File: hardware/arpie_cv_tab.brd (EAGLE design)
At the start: 35.9 x 57.2 mm, 63 parts, among them IC1 MCP4726, IC2 MCP601OT, IC3 LM27675M5_CHARGEPUMP, IC4 LM358D, IC5 LM4041A12DBZ, IC6 24LC_16BT-I/OT

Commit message: add values to schematic
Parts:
- R11, R8: value (none) -> 2m2
- R4, R5: value (none) -> 1k
- R6: value 100k -> 47k
- R7: value (none) -> 47k
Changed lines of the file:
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@@
 <attribute name="VALUE" x="82.804" y="31.496" size="1.27" layer="27" rot="R180"/>
 </element>
-<element name="R5" library="rcl" package="R0805" value="" x="81.915" y="22.86" smashed="yes">
+<element name="R5" library="rcl" package="R0805" value="1k" x="81.915" y="22.86" smashed="yes">
 <attribute name="NAME" x="77.597" y="22.987" size="1.27" layer="25" font="vector" ratio="20"/>
 </element>
-<element name="R4" library="rcl" package="R0805" value="" x="81.915" y="31.75" smashed="yes">
+<element name="R4" library="rcl" package="R0805" value="1k" x="81.915" y="31.75" smashed="yes">
 <attribute name="NAME" x="77.724" y="30.353" size="1.27" layer="25" font="vector" ratio="20"/>
 </element>
@@
 <attribute name="NAME" x="77.597" y="11.43" size="1.27" layer="25" font="vector" ratio="20" rot="R90"/>
 </element>
-<element name="R7" library="rcl" package="R0805" value="" x="67.31" y="15.24" smashed="yes" rot="R270">
+<element name="R7" library="rcl" package="R0805" value="47k" x="67.31" y="15.24" smashed="yes" rot="R270">
 <attribute name="NAME" x="64.77" y="11.938" size="1.27" layer="25" font="vector" ratio="20"/>
-<attribute name="VALUE" x="64.77" y="15.875" size="1.27" layer="27" rot="R270"/>
 </element>
-<element name="R6" library="rcl" package="R0805" value="100k" x="64.77" y="15.24" smashed="yes" rot="R90">
+<element name="R6" library="rcl" package="R0805" value="47k" x="64.77" y="15.24" smashed="yes" rot="R90">
 <attribute name="NAME" x="62.23" y="16.637" size="1.27" layer="25" font="vector" ratio="20" rot="R270"/>
 </element>
@@
 <attribute name="NAME" x="80.899" y="18.415" size="1.27" layer="25" font="vector" ratio="20"/>
 </element>
-<element name="R8" library="rcl" package="R0805" value="" x="79.375" y="16.129" smashed="yes" rot="R90">
+<element name="R8" library="rcl" package="R0805" value="2m2" x="79.375" y="16.129" smashed="yes" rot="R90">
 <attribute name="NAME" x="76.835" y="18.161" size="1.27" layer="25" font="vector" ratio="20" rot="R270"/>
-<attribute name="VALUE" x="81.915" y="15.494" size="1.27" layer="27" rot="R90"/>
 </element>
-<element name="R11" library="rcl" package="R0805" value="" x="79.375" y="8.89" smashed="yes" rot="R270">
+<element name="R11" library="rcl" package="R0805" value="2m2" x="79.375" y="8.89" smashed="yes" rot="R270">
 <attribute name="NAME" x="77.724" y="5.461" size="1.27" layer="25" font="vector" ratio="20"/>
-<attribute name="VALUE" x="76.835" y="9.525" size="1.27" layer="27" rot="R270"/>
 </element>
 <element name="C10" library="resistor" package="C0805" value="" x="69.85" y="15.24" smashed="yes" rot="R90">

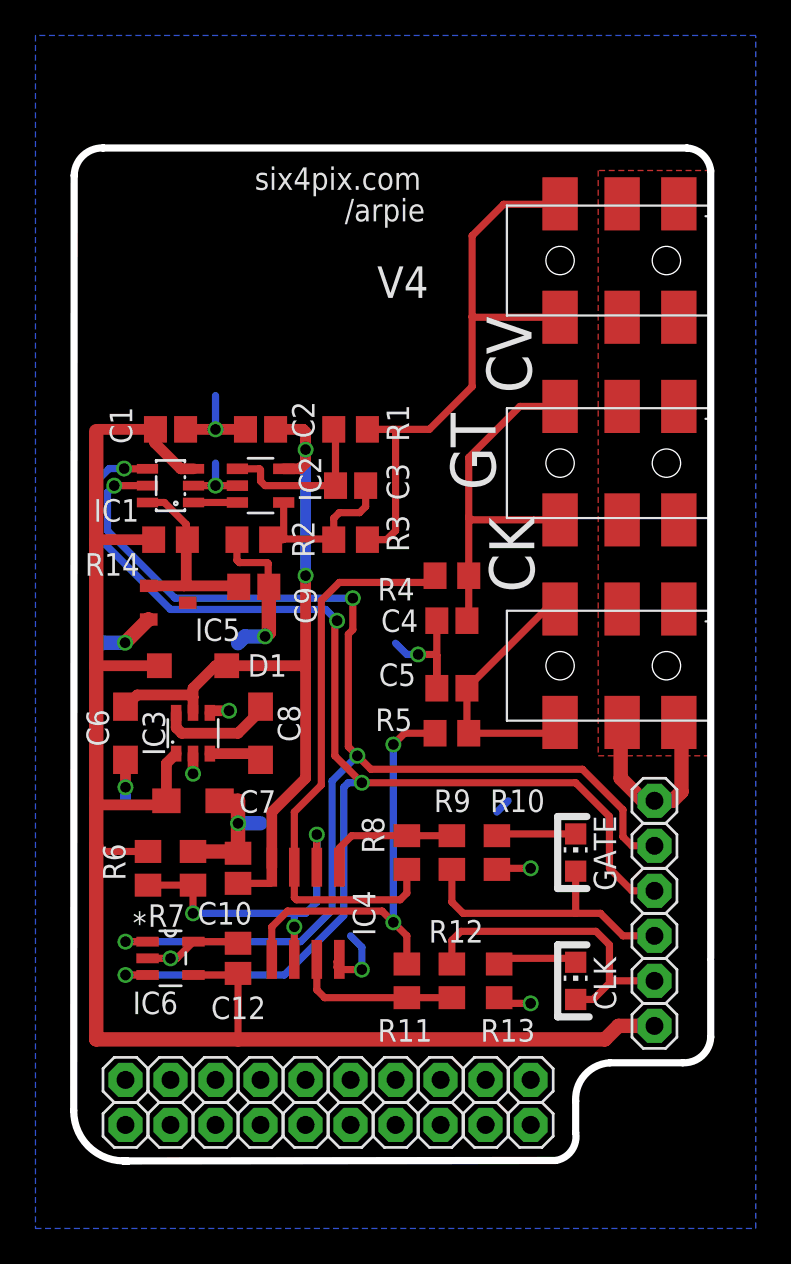
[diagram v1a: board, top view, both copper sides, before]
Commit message: V5 - change type of 3.5mm socket
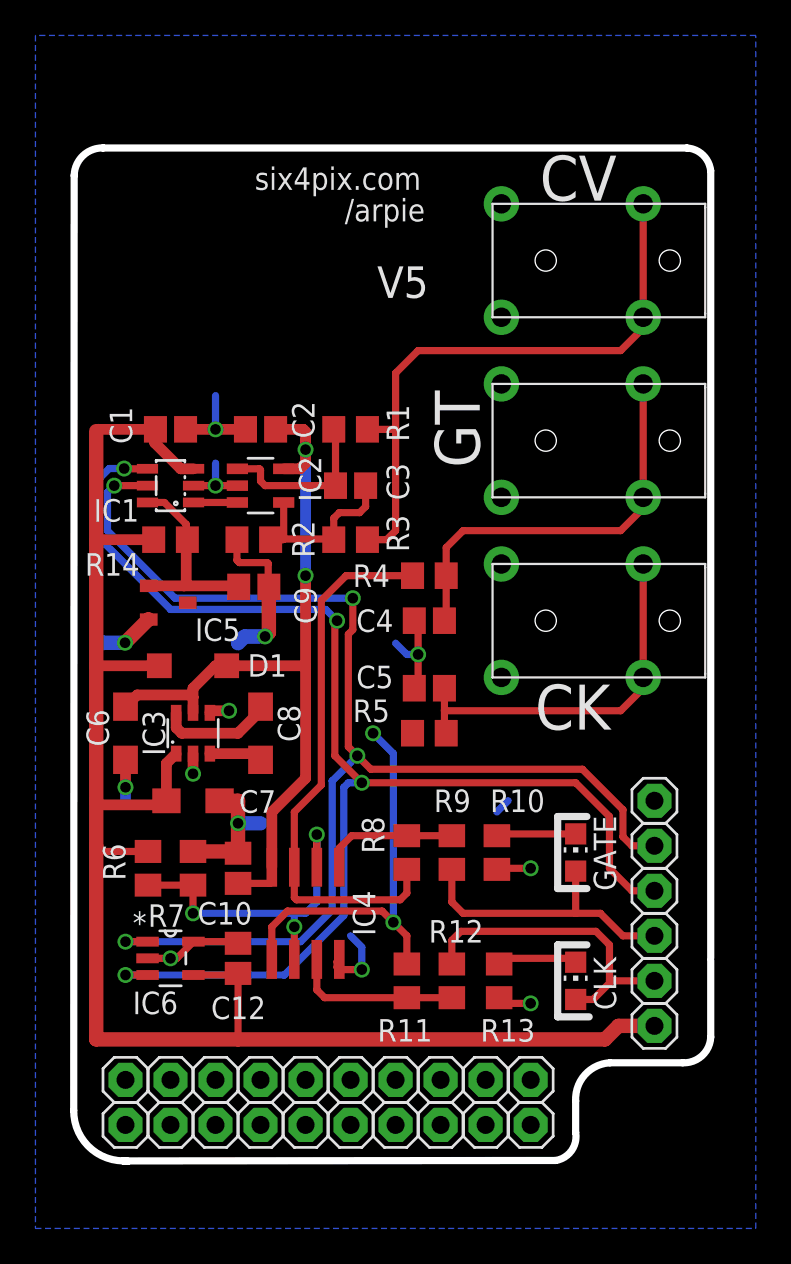
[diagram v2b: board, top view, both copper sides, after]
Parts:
- CLKOUT, CVOUT, GATEOUT: value SMD35MMJACK -> 3_5MM_PTH_MICRO; device jasons_stuff:SMD35MMJACK -> jason_eagle6:3_5MM_PTH_MICRO
- moved CLKOUT 4.58 mm to (92.7, 29.2), turned to 270 degrees
- moved GATEOUT 4.02 mm to (92.7, 39.4), turned to 270 degrees
- moved CVOUT 3.81 mm to (92.7, 49.5), turned to 270 degrees
- moved C4 1.27 mm to (80.6, 29.2)
- moved C5 1.27 mm to (80.6, 25.4)
- moved R4 1.27 mm to (80.6, 31.8)
- moved R5 1.27 mm to (80.6, 22.9)
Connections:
- net CVOUT: now also CVOUT.2, CVOUT.2A; no longer CVOUT.T, CVOUT.T@
- net GND: now also CLKOUT.1, CLKOUT.3, CVOUT.1, CVOUT.3, GATEOUT.1, GATEOUT.3; no longer CLKOUT.R, CLKOUT.R@, CLKOUT.S, CLKOUT.S@, CVOUT.R, CVOUT.R@, CVOUT.S, CVOUT.S@, GATEOUT.R, GATEOUT.R@, GATEOUT.S, GATEOUT.S@
- net N$19: now also CLKOUT.2, CLKOUT.2A; no longer CLKOUT.T, CLKOUT.T@
- net N$20: now also GATEOUT.2, GATEOUT.2A; no longer GATEOUT.T, GATEOUT.T@
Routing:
- net GND: track 68.7 -> 53.9 mm
- net N$19: track 15.1 -> 21.3 mm
- net N$20: track 20.8 -> 23.2 mm
- net N$9: track 24.6 -> 23.1 mm
- net N$12: track 32.3 -> 31.0 mm
- net CVOUT: track 33.6 -> 34.3 mm
- removed copper zone on layer 1, net GND
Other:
- board text added: "V5"
- board text removed: "V4"

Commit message: fix
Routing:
- net N$9: track 23.1 -> 25.4 mm
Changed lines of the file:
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@@
 <signal name="GND">
 <polygon width="0.4064" layer="16">
-<vertex x="58.42" y="62.23"/>
-<vertex x="58.42" y="-5.08"/>
-<vertex x="99.06" y="-5.08"/>
-<vertex x="99.06" y="62.23"/>
+<vertex x="60.96" y="55.88"/>
+<vertex x="60.96" y="-1.27"/>
+<vertex x="96.012" y="-1.27"/>
+<vertex x="96.012" y="55.88"/>
 </polygon>
 <contactref element="GND" pad="1"/>
@@
 <wire x1="78.613" y1="12.192" x2="78.613" y2="21.717" width="0.4064" layer="16"/>
 <wire x1="78.613" y1="21.717" x2="77.47" y2="22.86" width="0.4064" layer="16"/>
-<wire x1="78.613" y1="21.717" x2="79.695" y2="22.86" width="0" layer="19" extent="1-16"/>
+<wire x1="79.695" y1="22.86" x2="77.47" y2="22.86" width="0.4064" layer="1"/>
 </signal>
 <signal name="+10V">
